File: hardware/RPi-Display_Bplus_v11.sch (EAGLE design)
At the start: 59 parts, among them IC1 ADS7846, IC2 24LC-I/OT, IC3 LDO-TS9011-3V3, Q1 N-CHN, SW1 SW-TACTILE-PTS840P, SW2 SW-TACTILE-PTS840P, SW3 SW-TACTILE-PTS840P, X1 PASSER, X2 PASSER, X3 PASSER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

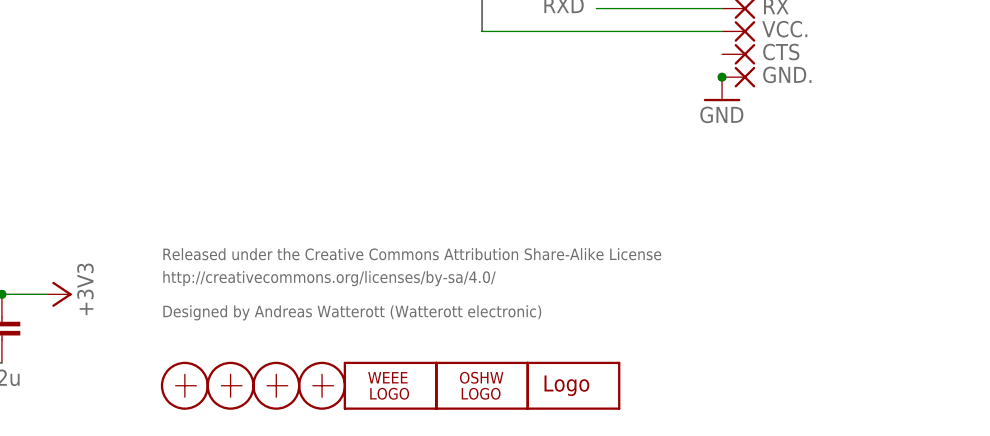
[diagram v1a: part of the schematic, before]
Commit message: updated schematics
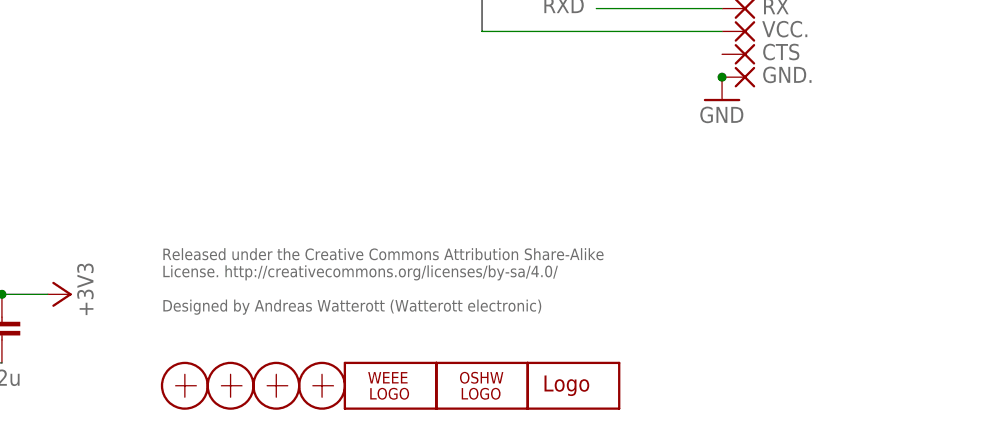
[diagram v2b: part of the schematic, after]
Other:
- note added: "Released under the Creative Commons Attribution Share-Alike License. http://creativecommons.org/licenses/by-sa/4.0/ Designed by Andreas Watterott (Watterott electronic)"
- note removed: "Designed by Andreas Watterott (Watterott electronic)"
- note removed: "Released under the Creative Commons Attribution Share-Alike License"
- note removed: "http://creativecommons.org/licenses/by-sa/4.0/"
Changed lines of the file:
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@@
 <setting verticaltext="up"/>
 </settings>
-<grid distance="0.1" unitdist="inch" unit="inch" style="lines" multiple="1" display="no" altdistance="0.01" altunitdist="inch" altunit="inch"/>
+<grid distance="0.05" unitdist="inch" unit="inch" style="lines" multiple="1" display="yes" altdistance="0.025" altunitdist="inch" altunit="inch"/>
 <layers>
 <layer number="1" name="Top" color="4" fill="1" visible="no" active="no"/>
@@
 <layer number="51" name="tDocu" color="7" fill="1" visible="no" active="no"/>
 <layer number="52" name="bDocu" color="7" fill="1" visible="no" active="no"/>
-<layer number="53" name="tCopper" color="7" fill="11" visible="no" active="no"/>
-<layer number="54" name="bCopper" color="7" fill="1" visible="no" active="no"/>
-<layer number="56" name="wert" color="7" fill="1" visible="no" active="no"/>
-<layer number="57" name="tCAD" color="7" fill="1" visible="no" active="no"/>
 <layer number="90" name="Modules" color="5" fill="1" visible="yes" active="yes"/>
 <layer number="91" name="Nets" color="2" fill="1" visible="yes" active="yes"/>
@@
 <layer number="98" name="Guide" color="6" fill="1" visible="yes" active="yes"/>
 <layer number="99" name="SpiceOrder" color="5" fill="1" visible="yes" active="yes"/>
-<layer number="100" name="Muster" color="7" fill="1" visible="no" active="no"/>
-<layer number="153" name="FabDoc1" color="6" fill="1" visible="no" active="no"/>
-<layer number="154" name="FabDoc2" color="2" fill="1" visible="no" active="no"/>
-<layer number="155" name="FabDoc3" color="7" fill="15" visible="no" active="no"/>
-<layer number="200" name="200bmp" color="1" fill="10" visible="no" active="no"/>
-<layer number="217" name="217bmp" color="18" fill="1" visible="no" active="no"/>
-<layer number="218" name="218bmp" color="19" fill="1" visible="no" active="no"/>
-<layer number="219" name="219bmp" color="20" fill="1" visible="no" active="no"/>
-<layer number="220" name="220bmp" color="21" fill="1" visible="no" active="no"/>
-<layer number="221" name="221bmp" color="22" fill="1" visible="no" active="no"/>
-<layer number="222" name="222bmp" color="23" fill="1" visible="no" active="no"/>
-<layer number="223" name="223bmp" color="24" fill="1" visible="no" active="no"/>
-<layer number="224" name="224bmp" color="25" fill="1" visible="no" active="no"/>
 <layer number="250" name="Descript" color="3" fill="1" visible="yes" active="yes"/>
-<layer number="251" name="SMDround" color="12" fill="11" visible="no" active="no"/>
 </layers>
 <schematic xreflabel="%F%N/%S.%C%R" xrefpart="/%S.%C%R">
@@
 <text x="31.75" y="167.64" size="3.81" layer="250">2.8" Display with Touchpanel</text>
 <text x="198.12" y="167.64" size="3.81" layer="250">Raspberry Pi B+</text>
-<text x="162.56" y="21.59" size="1.27" layer="95">Released under the Creative Commons Attribution Share-Alike License</text>
-<text x="162.56" y="19.05" size="1.27" layer="95">http://creativecommons.org/licenses/by-sa/4.0/</text>
-<text x="162.56" y="15.24" size="1.27" layer="95">Designed by Andreas Watterott (Watterott electronic)</text>
+<text x="162.56" y="22.86" size="1.27" layer="95" align="top-left">Released under the Creative Commons Attribution Share-Alike
+License. http://creativecommons.org/licenses/by-sa/4.0/
+Designed by Andreas Watterott (Watterott electronic)</text>
 <text x="115.57" y="105.41" size="3.81" layer="250">Touch Controller</text>
 <text x="127" y="64.77" size="1.778" layer="95">or TSC2046</text>
@@
 </schematic>
 </drawing>
+<compatibility>
+<note version="6.3" minversion="6.2.2" severity="warning">
+Since Version 6.2.2 text objects can contain more than one line,
+which will not be processed correctly with this version.
+</note>
+</compatibility>
 </eagle>
